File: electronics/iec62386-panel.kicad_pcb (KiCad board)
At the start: 2 copper layers, 43 x 43 mm, 61 parts, among them J1 Screw_Terminal_01x04, J2 Conn_01x10 8.5mm, J3 Conn_01x10 8.5mm, J4 Conn_01x02, J6 Conn_02x03_Counter_Clockwise, Q1 MMBT5551L, Q2 DMN62D0U, U2 TPS62932, U3 ENS210, U4 LPS22HH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

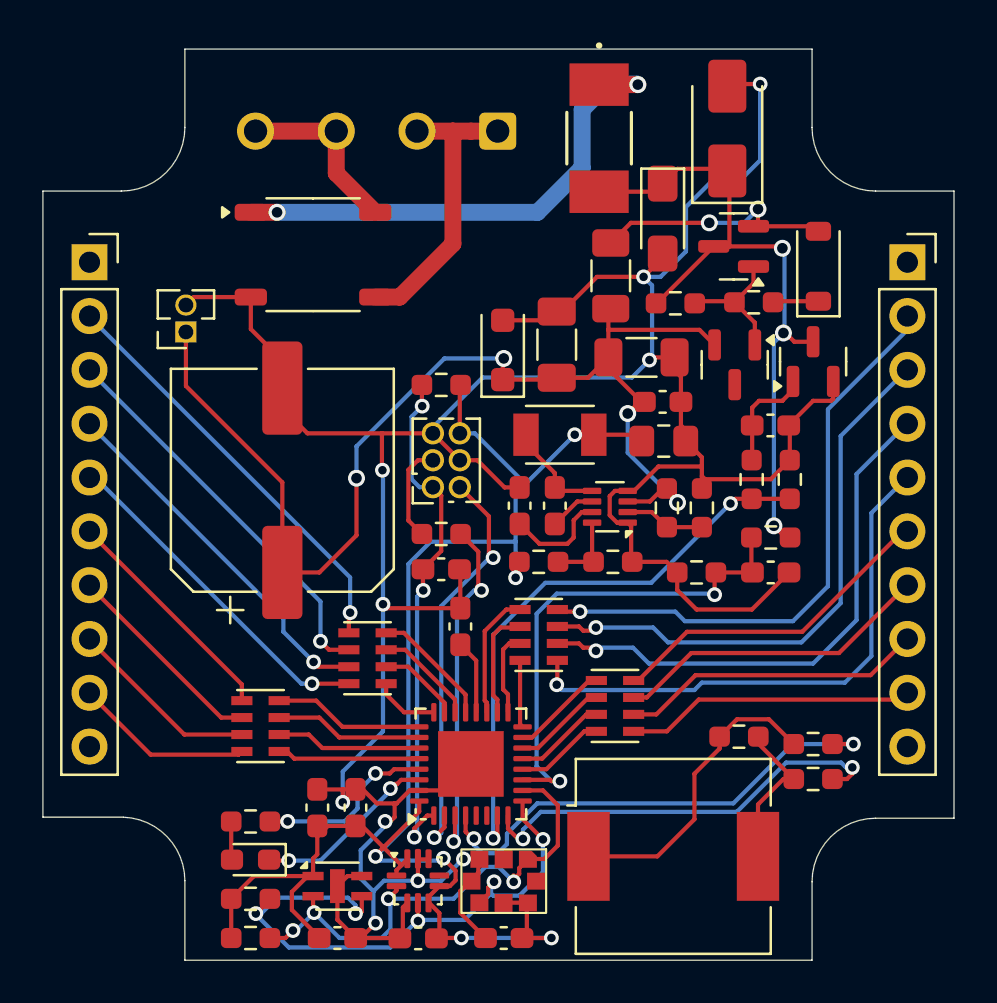
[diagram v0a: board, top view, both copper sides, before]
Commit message: Fixed errors of the first hw prototype
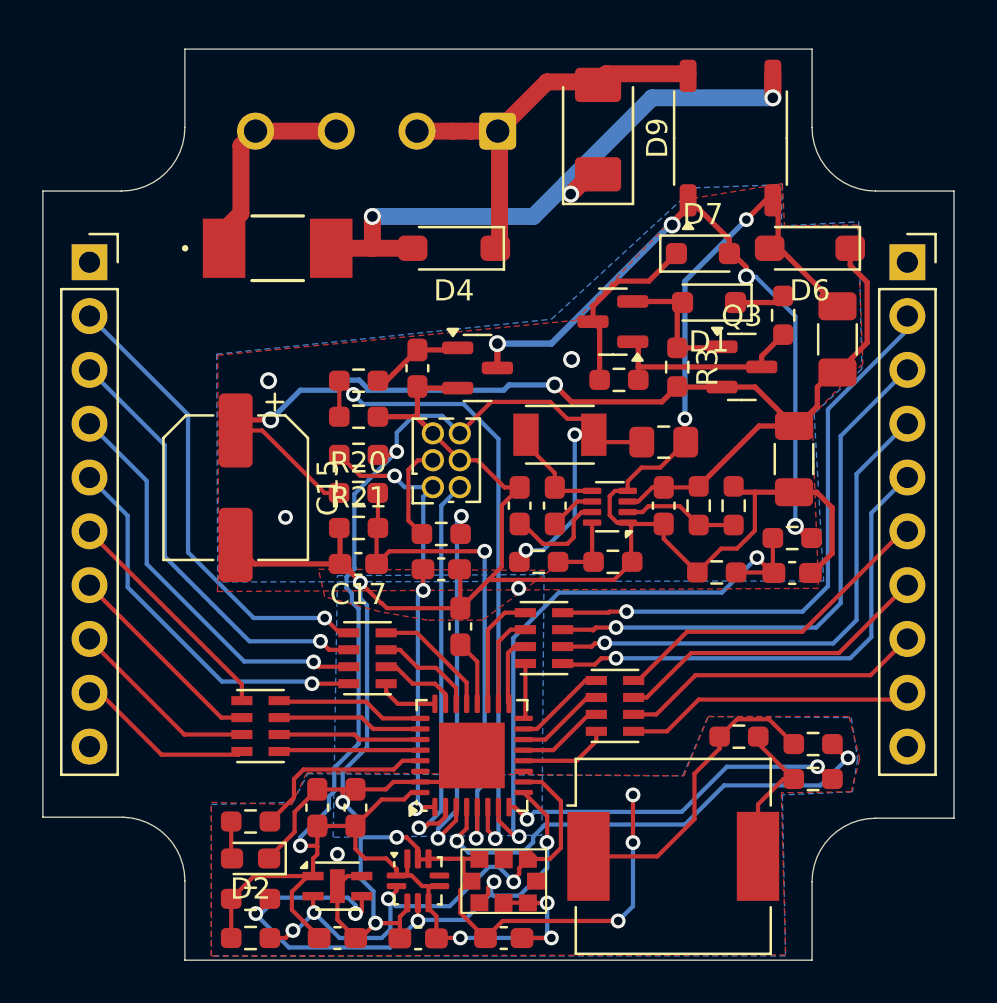
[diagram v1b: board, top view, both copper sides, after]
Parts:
- removed D3: 1N4148W, Diode_SMD:D_SOD-123
- removed D8: LTL-14CHJ, LED_SMD:LED_0603_1608Metric_Pad1.05x0.95mm_HandSolder
- removed J4: Conn_01x02, Connector_PinSocket_1.27mm:PinSocket_1x02_P1.27mm_Vertical
- added C17: 22pF, Capacitor_SMD:C_0603_1608Metric_Pad1.08x0.95mm_HandSolder, F.Cu at (101.6, 90.0)
- added D1: BAT54J, Diode_SMD:D_SOD-323_HandSoldering, F.Cu at (118.1, 77.7)
- added D9: MDB6S, Package_SO:TSSOP-4_4.4x5mm_P4mm, F.Cu at (119.2, 70.0)
- added Q3: MMBT5551L, Package_TO_SOT_SMD:SOT-23, F.Cu at (119.7, 80.8)
- added R20: 1M, Resistor_SMD:R_0603_1608Metric_Pad0.98x0.95mm_HandSolder, F.Cu at (101.6, 86.7)
- added R21: 100k, Resistor_SMD:R_0603_1608Metric_Pad0.98x0.95mm_HandSolder, F.Cu at (101.6, 88.3)
- C15: footprint Capacitor_SMD:CP_Elec_10x7.7 -> Capacitor_SMD:CP_Elec_6.3x7.7
- D2: value SMF33A -> LED; footprint Diode_SMD:D_SMF-DEBUG -> LED_SMD:LED_0603_1608Metric_Pad1.05x0.95mm_HandSolder
- D4: value BAV99 -> SMF33CA; footprint Package_TO_SOT_SMD:SOT-23 -> Diode_SMD:D_SOD-123-DEBUG
- D6: footprint Diode_SMD:D_SOD-123F -> Diode_SMD:D_SOD-123-DEBUG
- D7: value MDB6S -> BAT54J; footprint Package_SO:TSSOP-4_4.4x5mm_P4mm -> Diode_SMD:D_SOD-323_HandSoldering
- F1: value 0678H0500-023 500mA fast -> 0679H0375-05 375mA fast
- R15, R16: value 100 -> 0
- R3: footprint Resistor_SMD:R_1206_3216Metric_Pad1.30x1.75mm_HandSolder -> Resistor_SMD:R_0603_1608Metric_Pad0.98x0.95mm_HandSolder
- R7: value 3.6M -> 100k
- R8: value 400k -> 10k
- moved D2 35.9 mm to (96.5, 104.0), turned to 180 degrees
- moved R10 20.6 mm to (101.6, 83.1), turned to 0 degrees
- moved R9 19.1 mm to (101.6, 81.4), turned to 0 degrees
- moved D7 18.4 mm to (117.8, 75.4)
- moved C4 16.9 mm to (104.4, 80.8), turned to -90 degrees
- moved F1 16.0 mm to (97.8, 75.2), turned to 0 degrees
- moved Q2 15.8 mm to (107.2, 80.8), turned to 0 degrees
- moved D6 15.3 mm to (122.9, 75.2), turned to 180 degrees
- moved D4 14.3 mm to (106.1, 75.2), turned to 180 degrees
- moved C1 13.3 mm to (124.2, 79.5)
- moved C5 8.65 mm to (122.2, 85.1), turned to -90 degrees
- moved Q1 6.72 mm to (113.6, 78.6)
- moved D5 6.10 mm to (112.9, 69.5)
- moved R3 5.33 mm to (116.6, 80.8)
- moved R18 5.11 mm to (101.6, 84.9)
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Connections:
- D2 pad 1: VBUS -> GND
- D2 pad 2: GND -> Net-(D2-A)
- D4 pad 1: /IEC 62386 interface/HV_2 -> /IEC 62386 interface/BUS_2
- D4 pad 2: VS -> Net-(D4-A2)
- D5 pad 1: VBUS -> Net-(D4-A2)
- D5 pad 2: GND -> /IEC 62386 interface/BUS_2
- D7 pad 1: /IEC 62386 interface/BUS_+ -> Net-(D7-K)
- D7 pad 2: GND -> VBUS
- F1 pad 1: /IEC 62386 interface/BUS_+ -> /IEC 62386 interface/BUS_1
- F1 pad 2: VBUS -> Net-(D4-A2)
- Q1 pad 3: VBUS -> Net-(D7-K)
- R17 pad 2: Net-(D8-AK) -> Net-(D2-A)
- R2 pad 1: VBUS -> /IEC 62386 interface/HV_2
- R2 pad 2: /IEC 62386 interface/HV_2 -> Net-(D7-K)
- U6 pad 11: DALI_RX -> unconnected-(U6-P2.2_SYNC_ACLK_COMP0.1-Pad11)
- U6 pad 30: LED2 -> unconnected-(U6-P2.1_XIN-Pad30)
- U6 pad 5: unconnected-(U6-P1.6_UCA0CLK_TA1CLK_TDI_TCLK_A6-Pad5) -> VBUF_TEST
- U6 pad 6: unconnected-(U6-P1.7_UCA0STE_SMCLK_TDO_A7-Pad6) -> DALI_TX
- U6 pad 7: DALI_TX -> DALI_RX
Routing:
- net Net-(D4-A2): track 0.00 -> 29.8 mm, vias 0 -> 3
- net /IEC 62386 interface/BUS_+: track 24.2 -> 0.00 mm, vias 2 -> 0
- net VBUF_TEST: track 0.00 -> 23.9 mm, vias 0 -> 2
- net LED2: track 8.75 -> 0.00 mm, vias 2 -> 0
- net Net-(D7-K): track 0.00 -> 8.57 mm
- net +2V7: track 78.4 -> 85.4 mm, vias 6 -> 7
- net GND: track 159.5 -> 153.2 mm, vias 10 -> 14
- net /IEC 62386 interface/BUS_2: track 14.0 -> 19.6 mm
- net DALI_RX: track 23.8 -> 29.1 mm
- net /IEC 62386 interface/HV_1: track 11.7 -> 6.74 mm, vias 2 -> 0
- net DALI_TX: track 27.4 -> 30.9 mm
- net BUZZER2: track 20.3 -> 16.8 mm
- net /IEC 62386 interface/HV_2: track 6.37 -> 9.68 mm
- net Net-(J3-Pin_5): track 26.0 -> 23.5 mm
- net Net-(J2-Pin_5): track 16.3 -> 18.6 mm
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- added copper zone on B.Cu, net GND
- added copper zone on F.Cu, net GND
